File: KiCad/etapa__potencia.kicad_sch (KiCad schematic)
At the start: 8 parts

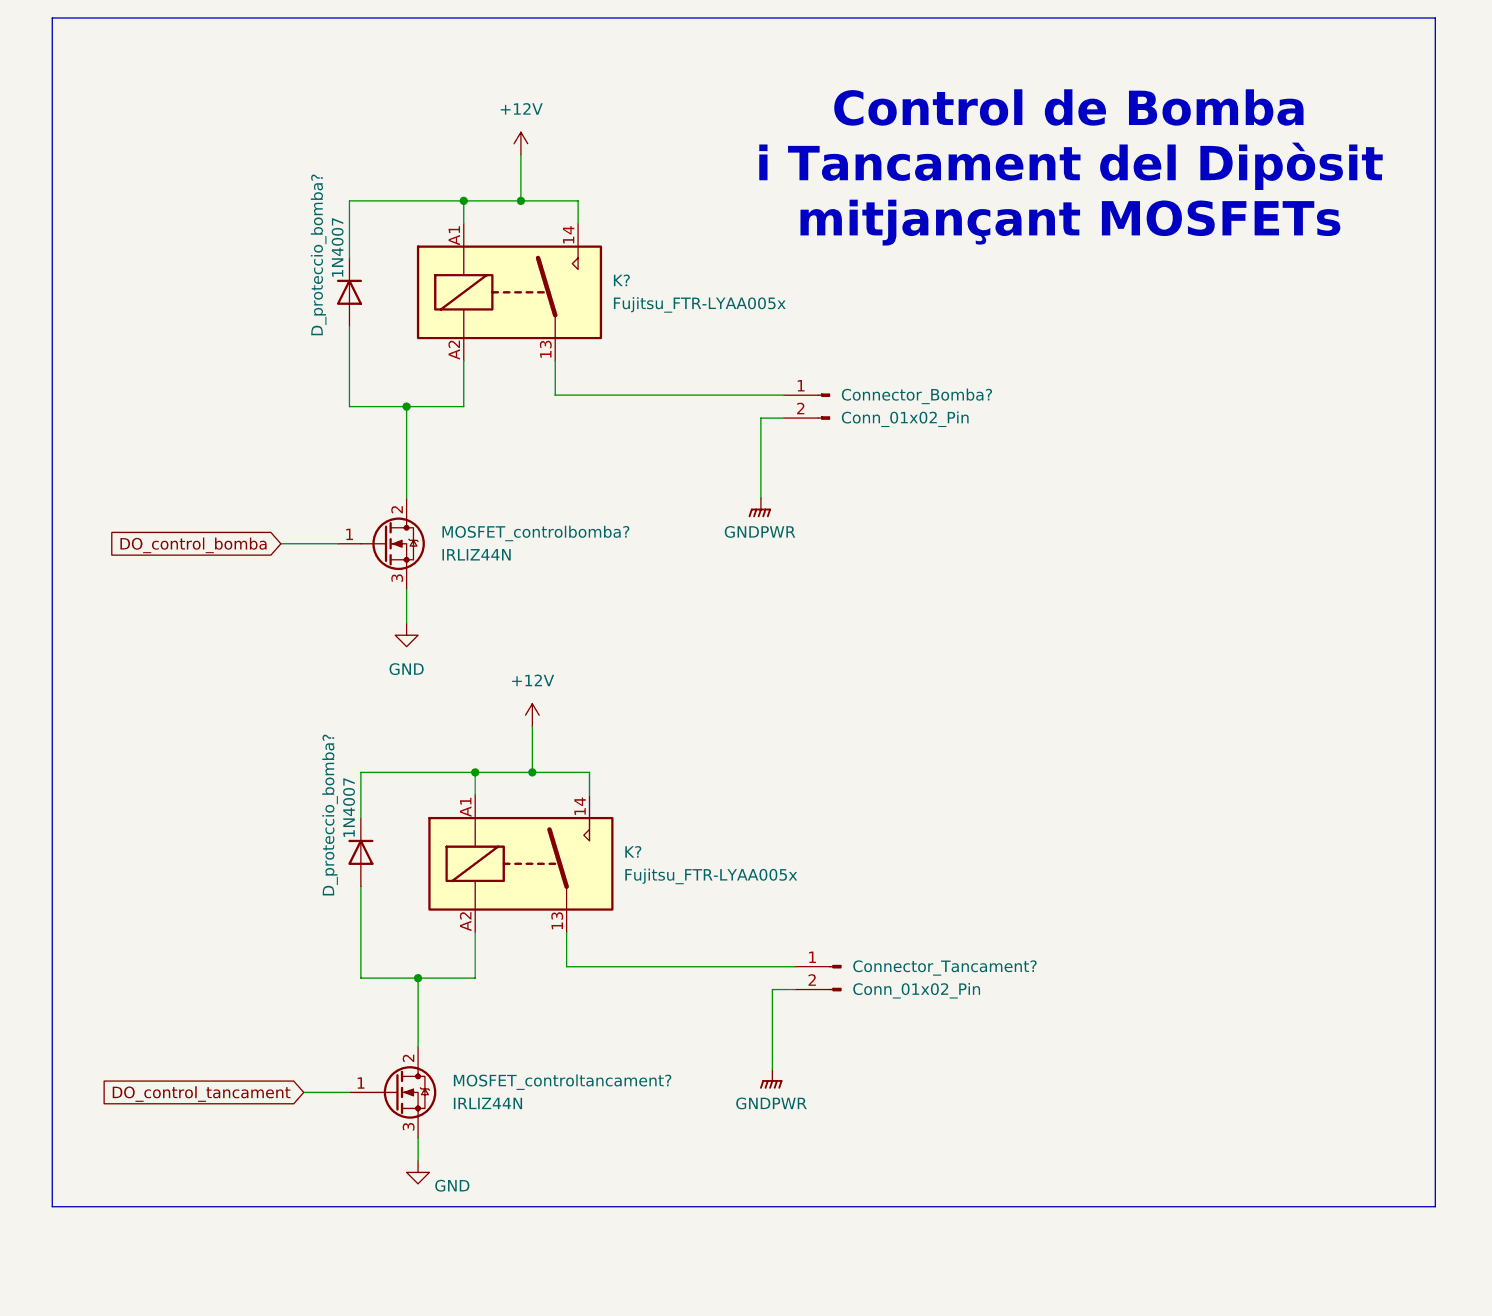
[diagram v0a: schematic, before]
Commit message: PCB avançada primer Placement (falten components passius)
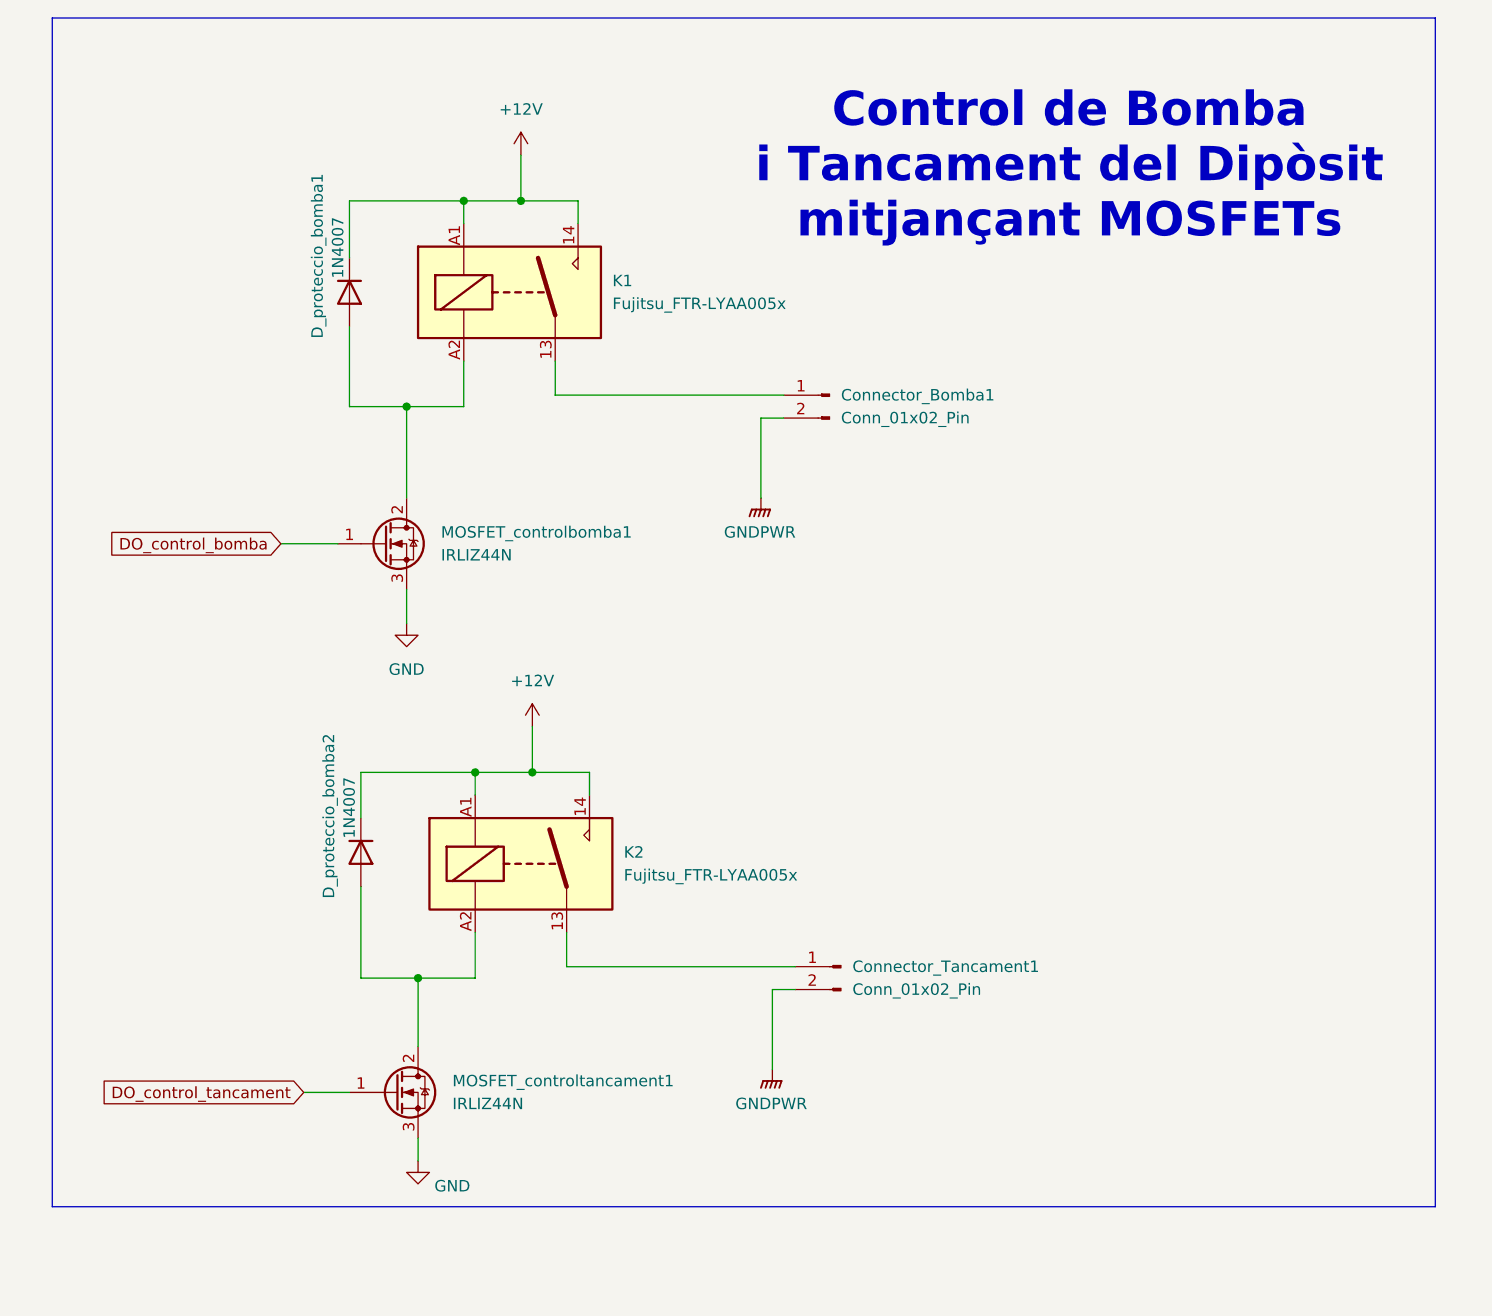
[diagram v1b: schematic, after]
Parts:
- gave numbers to parts that had none: 8
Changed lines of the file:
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@@
 		(dnp no)
 		(fields_autoplaced yes)
-		(property "Reference" "K?"
+		(property "Reference" "K2"
 			(at 88.9 118.1099 0)
 			(effects
@@
 			(project "PROJECTE_CASTRO_RIBAS"
 				(path "/27a7fca5-115a-450a-aa60-496c314f6c0e/2ae4c977-7e45-4d92-9ae0-450b29246e42"
-					(reference "K?")
+					(reference "K2")
 					(unit 1)
 				)
@@
 		(dnp no)
 		(fields_autoplaced yes)
-		(property "Reference" "K?"
+		(property "Reference" "K1"
 			(at 87.63 54.6099 0)
 			(effects
@@
 			(project "PROJECTE_CASTRO_RIBAS"
 				(path "/27a7fca5-115a-450a-aa60-496c314f6c0e/2ae4c977-7e45-4d92-9ae0-450b29246e42"
-					(reference "K?")
+					(reference "K1")
 					(unit 1)
 				)
@@
 		(dnp no)
 		(fields_autoplaced yes)
-		(property "Reference" "MOSFET_controlbomba?"
+		(property "Reference" "MOSFET_controlbomba1"
 			(at 68.58 82.5499 0)
 			(effects
@@
 			(project "PROJECTE_CASTRO_RIBAS"
 				(path "/27a7fca5-115a-450a-aa60-496c314f6c0e/2ae4c977-7e45-4d92-9ae0-450b29246e42"
-					(reference "MOSFET_controlbomba?")
+					(reference "MOSFET_controlbomba1")
 					(unit 1)
 				)
@@
 		(on_board yes)
 		(dnp no)
-		(property "Reference" "D_proteccio_bomba?"
+		(property "Reference" "D_proteccio_bomba1"
 			(at 54.864 42.672 0)
 			(effects
@@
 			(project "PROJECTE_CASTRO_RIBAS"
 				(path "/27a7fca5-115a-450a-aa60-496c314f6c0e/2ae4c977-7e45-4d92-9ae0-450b29246e42"
-					(reference "D_proteccio_bomba?")
+					(reference "D_proteccio_bomba1")
 					(unit 1)
 				)
@@
 		(dnp no)
 		(fields_autoplaced yes)
-		(property "Reference" "Connector_Tancament?"
+		(property "Reference" "Connector_Tancament1"
 			(at 114.3 130.8099 0)
 			(effects
@@
 			(project "PROJECTE_CASTRO_RIBAS"
 				(path "/27a7fca5-115a-450a-aa60-496c314f6c0e/2ae4c977-7e45-4d92-9ae0-450b29246e42"
-					(reference "Connector_Tancament?")
+					(reference "Connector_Tancament1")
 					(unit 1)
 				)
@@
 		(dnp no)
 		(fields_autoplaced yes)
-		(property "Reference" "Connector_Bomba?"
+		(property "Reference" "Connector_Bomba1"
 			(at 113.03 67.3099 0)
 			(effects
@@
 			(project "PROJECTE_CASTRO_RIBAS"
 				(path "/27a7fca5-115a-450a-aa60-496c314f6c0e/2ae4c977-7e45-4d92-9ae0-450b29246e42"
-					(reference "Connector_Bomba?")
+					(reference "Connector_Bomba1")
 					(unit 1)
 				)
@@
 		(on_board yes)
 		(dnp no)
-		(property "Reference" "MOSFET_controltancament?"
+		(property "Reference" "MOSFET_controltancament1"
 			(at 69.85 143.5099 0)
 			(effects
@@
 			(project "PROJECTE_CASTRO_RIBAS"
 				(path "/27a7fca5-115a-450a-aa60-496c314f6c0e/2ae4c977-7e45-4d92-9ae0-450b29246e42"
-					(reference "MOSFET_controltancament?")
+					(reference "MOSFET_controltancament1")
 					(unit 1)
 				)
@@
 		(dnp no)
 		(fields_autoplaced yes)
-		(property "Reference" "#PWR?"
+		(property "Reference" "#PWR0114"
 			(at 77.47 44.45 0)
 			(effects
@@
 			(project "PROJECTE_CASTRO_RIBAS"
 				(path "/27a7fca5-115a-450a-aa60-496c314f6c0e/2ae4c977-7e45-4d92-9ae0-450b29246e42"
-					(reference "#PWR?")
+					(reference "#PWR0114")
 					(unit 1)
 				)
@@
 		(dnp no)
 		(fields_autoplaced yes)
-		(property "Reference" "#PWR?"
+		(property "Reference" "#PWR0116"
 			(at 105.41 147.32 0)
 			(effects
@@
 			(project "PROJECTE_CASTRO_RIBAS"
 				(path "/27a7fca5-115a-450a-aa60-496c314f6c0e/2ae4c977-7e45-4d92-9ae0-450b29246e42"
-					(reference "#PWR?")
+					(reference "#PWR0116")
 					(unit 1)
 				)
@@
 		(on_board yes)
 		(dnp no)
-		(property "Reference" "D_proteccio_bomba?"
+		(property "Reference" "D_proteccio_bomba2"
 			(at 56.134 104.902 0)
 			(effects
@@
 			(project "PROJECTE_CASTRO_RIBAS"
 				(path "/27a7fca5-115a-450a-aa60-496c314f6c0e/2ae4c977-7e45-4d92-9ae0-450b29246e42"
-					(reference "D_proteccio_bomba?")
+					(reference "D_proteccio_bomba2")
 					(unit 1)
 				)
@@
 		(dnp no)
 		(fields_autoplaced yes)
-		(property "Reference" "#PWR?"
+		(property "Reference" "#PWR0115"
 			(at 64.77 99.06 0)
 			(effects
@@
 			(project "PROJECTE_CASTRO_RIBAS"
 				(path "/27a7fca5-115a-450a-aa60-496c314f6c0e/2ae4c977-7e45-4d92-9ae0-450b29246e42"
-					(reference "#PWR?")
+					(reference "#PWR0115")
 					(unit 1)
 				)
@@
 		(dnp no)
 		(fields_autoplaced yes)
-		(property "Reference" "#PWR?"
+		(property "Reference" "#PWR0113"
 			(at 78.74 107.95 0)
 			(effects
@@
 			(project "PROJECTE_CASTRO_RIBAS"
 				(path "/27a7fca5-115a-450a-aa60-496c314f6c0e/2ae4c977-7e45-4d92-9ae0-450b29246e42"
-					(reference "#PWR?")
+					(reference "#PWR0113")
 					(unit 1)
 				)
@@
 		(dnp no)
 		(fields_autoplaced yes)
-		(property "Reference" "#PWR?"
+		(property "Reference" "#PWR0112"
 			(at 104.14 83.82 0)
 			(effects
@@
 			(project "PROJECTE_CASTRO_RIBAS"
 				(path "/27a7fca5-115a-450a-aa60-496c314f6c0e/2ae4c977-7e45-4d92-9ae0-450b29246e42"
-					(reference "#PWR?")
+					(reference "#PWR0112")
 					(unit 1)
 				)
@@
 		(on_board yes)
 		(dnp no)
-		(property "Reference" "#PWR?"
+		(property "Reference" "#PWR0117"
 			(at 66.04 158.75 0)
 			(effects
@@
 			(project "PROJECTE_CASTRO_RIBAS"
 				(path "/27a7fca5-115a-450a-aa60-496c314f6c0e/2ae4c977-7e45-4d92-9ae0-450b29246e42"
-					(reference "#PWR?")
-					(unit 1)
-				)
+					(reference "#PWR0117")
+					(unit 1)
+				)

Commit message: ALFRED DEGANOS SECOOOOS PLS DADDY ALFRED TE CAMELAMOS
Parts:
- added TP8: Tp_12V_Bomba, TestPoint:TestPoint_Keystone_5015_Micro_Mini, symbol Connector:TestPoint
- added TP9: Tp_12V_Tancament, TestPoint:TestPoint_Keystone_5015_Micro_Mini, symbol Connector:TestPoint
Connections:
- net +12V: now also TP8.1, TP9.1
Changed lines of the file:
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@@
+	)
+	(junction
+		(at 83.82 45.72)
+		(diameter 0)
+		(color 0 0 0 0)
 	)
 	(junction
 		(at 66.04 132.08)
+		(diameter 0)
+		(color 0 0 0 0)
+	)
+	(junction
+		(at 85.09 109.22)
 		(diameter 0)
 		(color 0 0 0 0)
@@
 	)
 	(symbol
+		(lib_id "Connector:TestPoint")
+		(at 83.82 45.72 0)
+		(unit 1)
+		(exclude_from_sim no)
+		(in_bom yes)
+		(on_board yes)
+		(dnp no)
+		(property "Reference" "TP8"
+			(at 88.646 40.132 90)
+			(effects
+				(font
+					(size 1.27 1.27)
+				)
+			)
+		)
+		(property "Value" "Tp_12V_Bomba"
+			(at 86.106 40.132 90)
+			(effects
+				(font
+					(size 1.27 1.27)
+				)
+			)
+		)
+		(property "Footprint" "TestPoint:TestPoint_Keystone_5015_Micro_Mini"
+			(at 88.9 45.72 0)
+			(effects
+				(font
+					(size 1.27 1.27)
+				)
+				(hide yes)
+			)
+		)
+		(property "Datasheet" "~"
+			(at 88.9 45.72 0)
+			(effects
+				(font
+					(size 1.27 1.27)
+				)
+				(hide yes)
+			)
+		)
+		(property "Description" "test point"
+			(at 83.82 45.72 0)
+			(effects
+				(font
+					(size 1.27 1.27)
+				)
+				(hide yes)
+			)
+		)
+		(pin "1"
+		)
+		(instances
+			(project "PROJECTE_CASTRO_RIBAS"
+				(path "/27a7fca5-115a-450a-aa60-496c314f6c0e/2ae4c977-7e45-4d92-9ae0-450b29246e42"
+					(reference "TP8")
+					(unit 1)
+				)
+			)
+		)
+	)
+	(symbol
 		(lib_id "power:GND")
 		(at 64.77 92.71 0)
@@
 					(unit 1)
 				)
+			)
+		)
+	)
+	(symbol
+		(lib_id "Connector:TestPoint")
+		(at 85.09 109.22 0)
+		(unit 1)
+		(exclude_from_sim no)
+		(in_bom yes)
+		(on_board yes)
+		(dnp no)
+		(property "Reference" "TP9"
+			(at 89.916 103.632 90)
+			(effects
+				(font
+					(size 1.27 1.27)
+				)
+			)
+		)
+		(property "Value" "Tp_12V_Tancament"
+			(at 87.376 103.632 90)
+			(effects
+				(font
+					(size 1.27 1.27)
+				)
+			)
+		)
+		(property "Footprint" "TestPoint:TestPoint_Keystone_5015_Micro_Mini"
+			(at 90.17 109.22 0)
+			(effects
+				(font
+					(size 1.27 1.27)
+				)
+				(hide yes)
+			)
+		)
+		(property "Datasheet" "~"
+			(at 90.17 109.22 0)
+			(effects
+				(font
+					(size 1.27 1.27)
+				)
+				(hide yes)
+			)
+		)
+		(property "Description" "test point"
+			(at 85.09 109.22 0)
+			(effects
+				(font
+					(size 1.27 1.27)
+				)
+				(hide yes)
+			)
+		)
+		(pin "1"
+		)
+		(instances
+			(project "PROJECTE_CASTRO_RIBAS"
+				(path "/27a7fca5-115a-450a-aa60-496c314f6c0e/2ae4c977-7e45-4d92-9ae0-450b29246e42"
+					(reference "TP9")
+					(unit 1)
+				)
